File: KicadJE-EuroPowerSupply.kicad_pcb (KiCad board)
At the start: 2 copper layers, 100 x 100 mm, 115 parts, among them J101 Laptop Power, J102 +-15V thru, J103 +-12v out, J104 +5V out, J105 Laptop Power Out, P101 Doepfer_Power_10pin, P102 Doepfer_Power_16pin, P103 Doepfer_Power_10pin, P104 Doepfer_Power_16pin, P105 Doepfer_Power_10pin, P106 Doepfer_Power_16pin, P107 Doepfer_Power_10pin, P108 Doepfer_Power_16pin, Q201 TIP41, Q202 TIP41, Q203 TIP42, SW101 SW_SPDT, U201 LM7812_TO220, U202 LM7805_TO220, U203 Step Down Module +15 to 7v - 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, U204 LM7912_TO220, U205 XL6009 Module DCDC 19 to 30v, U206 TL071, U207 LM78M05_TO252, U208 LM78M12_TO252, U209 MC79M12_TO252, U210 MT3608 Module DCDC 19 to 28v

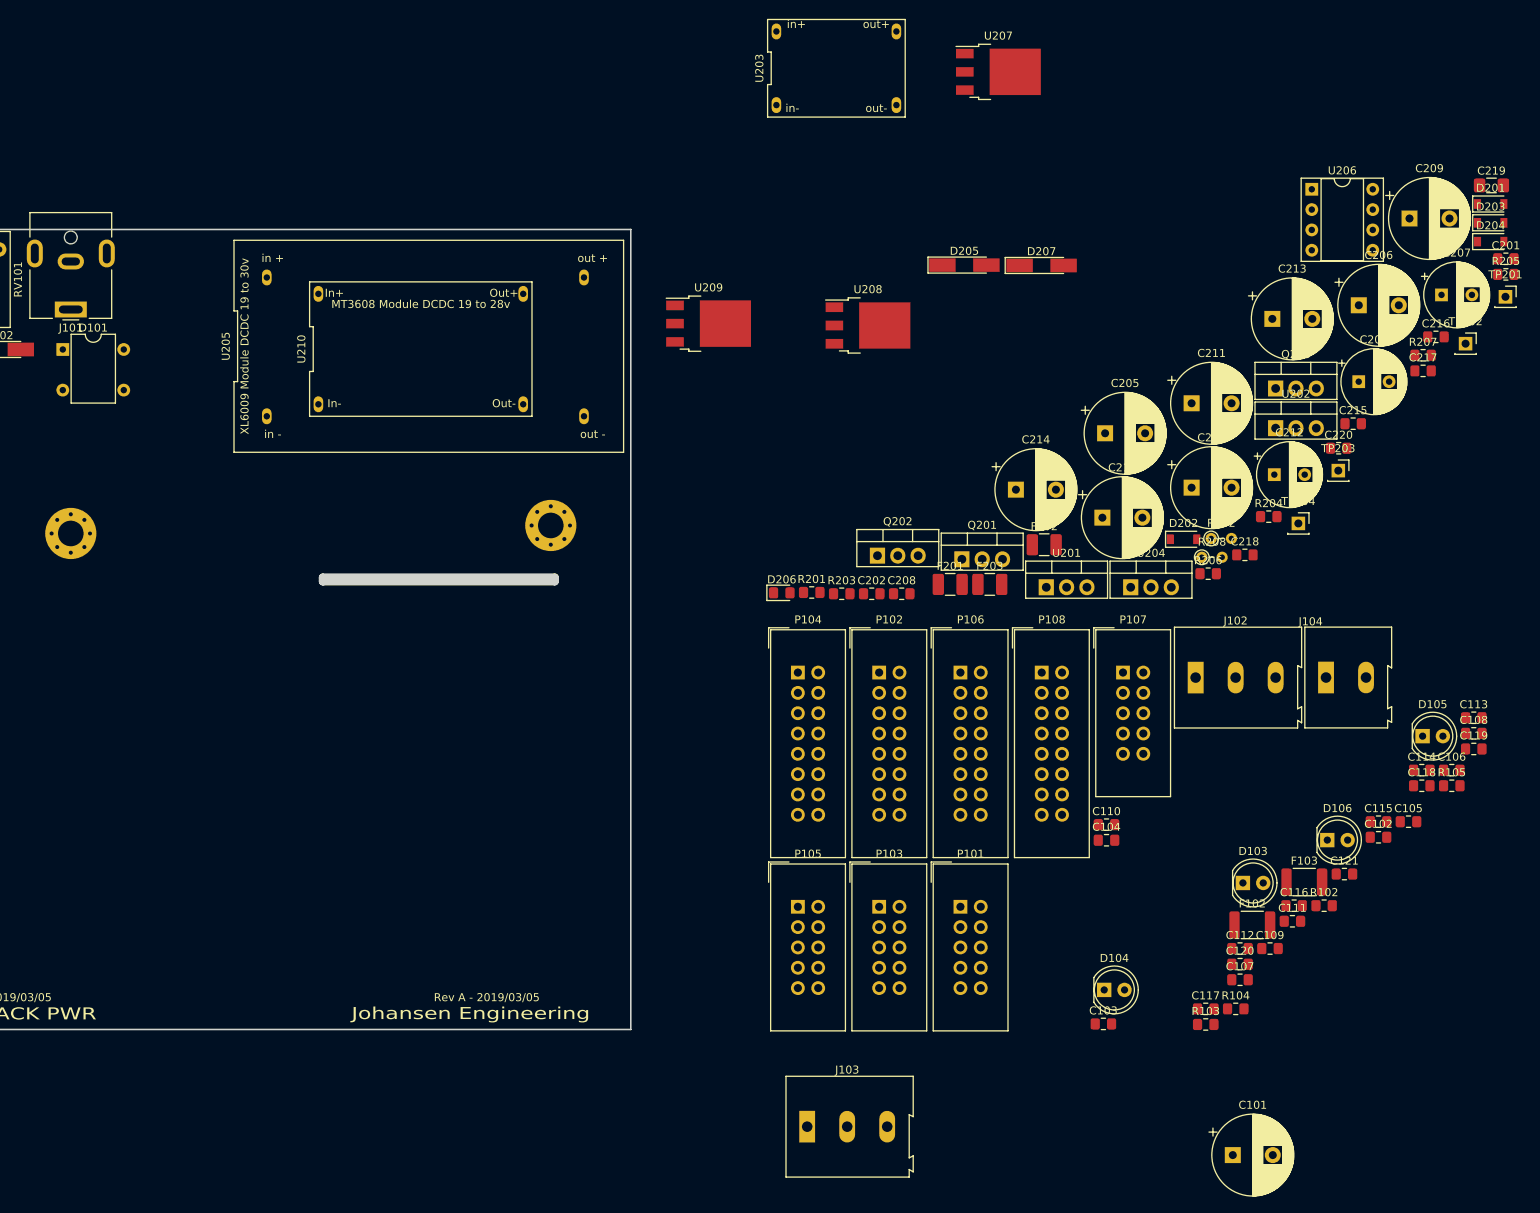
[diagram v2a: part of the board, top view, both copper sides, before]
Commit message: cut down to 2x10p and 2x16p
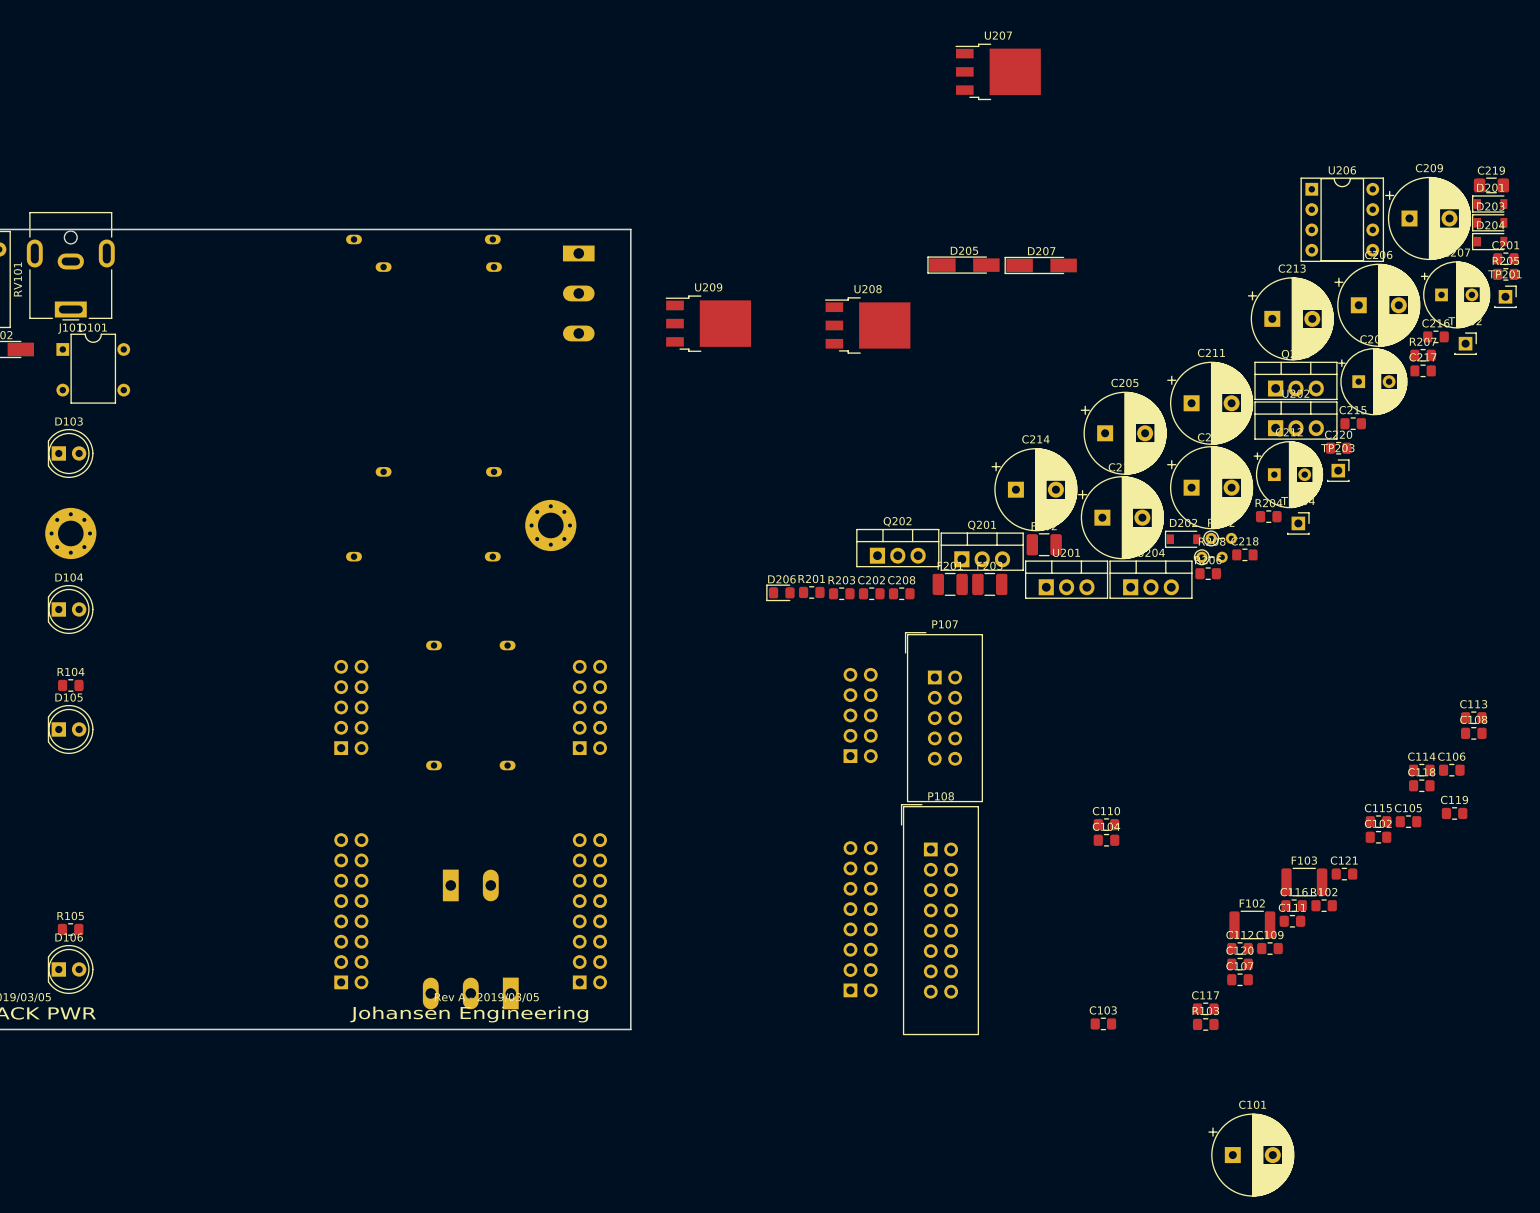
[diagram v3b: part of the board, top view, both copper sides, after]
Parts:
- J102, J103, J104, P101, P102, P103, P104, P105, P106, U203, U205, U210: moved to B.Cu
- moved R105 173.6 mm to (130.0, 137.5)
- moved D105 170.5 mm to (128.5, 112.5)
- moved D106 159.4 mm to (128.5, 142.5)
- moved D103 157.5 mm to (128.5, 78.0)
- moved R104 151.1 mm to (130.0, 107.0)
- moved D104 139.1 mm to (128.5, 97.5)
- moved J104 112.5 mm to (177.5, 132.0)
- moved J102 93.6 mm to (193.5, 53.0), turned to 270 degrees
- moved U203 91.8 mm to (180.0, 109.5), turned to 270 degrees
- moved P104 69.0 mm to (163.8, 144.1)
- moved P106 61.4 mm to (193.6, 144.1)
- moved P105 60.4 mm to (163.8, 114.8)
- moved P101 51.6 mm to (193.6, 114.8)
- moved J103 40.6 mm to (185.0, 145.5), turned to 180 degrees
- moved P102 39.9 mm to (227.5, 145.1)
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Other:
- outline, holes or cut-outs redrawn

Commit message: 3D Jigzaw started 90degr
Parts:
- removed C106, C107, C108, C109, C110, C111, C118, C119, C120, C121: 100n, Capacitor_SMD:C_0805_2012Metric_Pad1.15x1.40mm_HandSolder
- removed C211, C213: 1000uF, Capacitor_THT:CP_Radial_D10.0mm_P5.00mm
- removed P103, P107: Doepfer_Power_10pin, Connectors_IDC:IDC-Header_2x05_Pitch2.54mm_Straight
- removed P104, P108: Doepfer_Power_16pin, Connectors_IDC:IDC-Header_2x08_Pitch2.54mm_Straight
- removed REF** (x2): MountingHole_3.2mm_M3_Pad_Via, MountingHole:MountingHole_3.2mm_M3_Pad_Via
- added FL201: EMI_Filter_CommonMode, Inductor_THT:L_CommonMode_Toroid_Vertical_L19.3mm_W10.8mm_Px6.35mm_Py15.24mm_Bourns_8100, F.Cu at (99.0, -26.0)
- added FL202: EMI_Filter_CommonMode, Inductor_THT:L_CommonMode_Toroid_Vertical_L19.3mm_W10.8mm_Px6.35mm_Py15.24mm_Bourns_8100, F.Cu at (186.0, -25.5)
- added FL203: EMI_Filter_CommonMode, Inductor_THT:L_CommonMode_Toroid_Vertical_L19.3mm_W10.8mm_Px6.35mm_Py15.24mm_Bourns_8100, F.Cu at (140.7, -25.0)
- C203, C205, C210: value 1000uF -> 1u; footprint Capacitor_THT:CP_Radial_D10.0mm_P5.00mm -> Capacitor_SMD:C_1206_3216Metric_Pad1.42x1.75mm_HandSolder
- D206, R205: moved to B.Cu
- moved C201 241.3 mm to (95.0, -57.0)
- moved D201 237.2 mm to (96.0, -60.5)
- moved C204 226.9 mm to (92.0, -40.0)
- moved U201 216.5 mm to (93.4, -52.8)
- moved C206 212.0 mm to (104.0, -40.5)
- moved F201 208.7 mm to (103.5, -63.5)
- moved D203 208.6 mm to (139.5, -74.5), turned to 180 degrees
- moved F203 206.1 mm to (139.0, -82.5)
- moved U204 204.9 mm to (134.5, -65.3)
- moved C203 203.9 mm to (100.5, -31.0)
- moved TP202 196.0 mm to (112.0, 26.5)
- moved TP201 193.0 mm to (118.5, 29.5)
- moved C212 187.4 mm to (140.0, -43.5)
- moved TP203 179.6 mm to (118.5, 22.0)
- moved C215 179.5 mm to (149.0, -36.5)
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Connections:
- C205 pad 1: Net-(C205-Pad1) -> /VoltageRegulation/7V
- C205 pad 2: GND -> /VoltageRegulation/GND-7V
- C206 pad 1: Net-(C205-Pad1) -> +12V
- C208 pad 1: Net-(C208-Pad1) -> 5Vreg
- C210 pad 1: /VoltageRegulation/7V -> VinGND
- C210 pad 2: /VoltageRegulation/GND-7V -> Vin-15
- C214 pad 2: Net-(C213-Pad2) -> -12V
- D201 pad 2: Net-(C205-Pad1) -> 12Vreg
- D202 pad 2: Net-(C208-Pad1) -> 5Vreg
- D203 pad 1: Net-(C213-Pad2) -> -12Vreg
- F201 pad 1: Net-(C205-Pad1) -> 12Vreg
- F201 pad 2: Net-(C205-Pad1) -> +12V
- F202 pad 1: Net-(C208-Pad1) -> 5Vreg
- F203 pad 1: Net-(C213-Pad2) -> -12Vreg
- F203 pad 2: Net-(C213-Pad2) -> -12V
- U201 pad 3: Net-(C205-Pad1) -> 12Vreg
- U202 pad 3: Net-(C208-Pad1) -> 5Vreg
- U204 pad 3: Net-(C213-Pad2) -> -12Vreg
- U207 pad 3: +5V -> 5Vreg
- U208 pad 3: +12V -> 12Vreg
- U209 pad 3: -12V -> -12Vreg
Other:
- outline, holes or cut-outs redrawn

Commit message: Update KicadJE-EuroPowerSupply.kicad_pcb
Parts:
- added J106: FrontInterConnVin, AJ-Dropbox-Kicad:BoardConnector2x2.54x10mm2pin, F.Cu at (146.8, 85.8)
- added J107: BaseInterConnVin, AJ-Dropbox-Kicad:BoardConnector2x2.54x10mm2pin, F.Cu at (121.2, 85.6)
- added J108: FrontInterConnVout, AJ-Dropbox-Kicad:BoardConnector2x2.54x10mm4pin, F.Cu at (146.8, 129.1)
- added J109: BaseInterConnVout, AJ-Dropbox-Kicad:BoardConnector2x2.54x10mm4pin, F.Cu at (121.2, 129.1)
- moved C202 173.3 mm to (254.5, 134.3)
- moved C205 173.3 mm to (237.5, 117.3)
- moved C207 173.3 mm to (252.8, 123.5)
- moved C209 173.3 mm to (239.5, 128.8)
- moved FL202 173.3 mm to (233.0, 141.3)
- moved C216 59.2 mm to (235.5, 57.5)
- moved C217 59.2 mm to (237.5, 32.5)
- moved C220 59.2 mm to (246.0, 47.3)
- moved Q202 59.2 mm to (233.3, 40.8)
- moved Q203 59.2 mm to (254.5, 41.0)
- moved R202 59.2 mm to (246.0, 22.6)
- moved R204 59.2 mm to (253.2, 19.9)
- moved R206 59.2 mm to (245.7, 27.0)
- moved R207 59.2 mm to (237.5, 61.5)
- moved R208 59.2 mm to (244.9, 25.0)
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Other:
- board text added: "EURORACK PWR19"
- board text removed: "EURORACK PWR"

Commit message: Init wiring
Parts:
- added REF**: BoardConnector2x2.54x10mm2pin, AJ-Dropbox-Kicad:BoardConnector2x2.54x10mm2pin, F.Cu at (0.00, 0.00)
- moved FL202 22.6 mm to (224.0, 162.0), turned to 180 degrees
- moved J101 20.0 mm to (110.0, 60.4)
- moved J105 20.0 mm to (130.0, 60.4)
- moved F101 13.0 mm to (120.0, 66.0), turned to 0 degrees
- moved D102 10.8 mm to (117.0, 55.0), turned to 90 degrees
- moved D101 7.28 mm to (127.0, 72.0), turned to 90 degrees
- moved R101 4.24 mm to (117.0, 62.0), turned to 90 degrees
- moved U205 1.30 mm to (164.8, 74.5)
- moved J107 1.00 mm to (122.2, 85.6)
- moved J109 1.00 mm to (122.2, 129.1)
- moved RV101 1.00 mm to (120.0, 60.0)
- moved R102 0.71 mm to (136.0, 77.0), turned to 270 degrees
- moved J106 0.27 mm to (146.8, 85.5), turned to 270 degrees
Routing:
- net Net-(D101-Pad3): track 0.00 -> 49.4 mm
- net Net-(D103-Pad2): track 0.00 -> 4.97 mm
- net Net-(D102-Pad1): track 0.00 -> 3.23 mm

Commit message: Update KicadJE-EuroPowerSupply.kicad_pcb
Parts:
- moved C112 34.0 mm to (181.5, 119.8), turned to 90 degrees
- moved C103 30.9 mm to (190.3, 95.5)
- moved C116 29.6 mm to (190.3, 103.0), turned to 90 degrees
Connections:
- net Net-(D101-Pad3) renamed /DCSleeve
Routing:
- net +12V: track 0.00 -> 136.2 mm, vias 0 -> 2
- net +5V: track 0.00 -> 55.4 mm, vias 0 -> 2
- net -12V: track 0.00 -> 37.4 mm
- net Net-(F101-Pad1): track 0.00 -> 34.9 mm
- net Net-(D101-Pad4): track 0.00 -> 33.7 mm
- net Vin-Pos19: track 0.00 -> 27.6 mm
- net Vin-Neg19: track 0.00 -> 22.5 mm
- net Net-(J101-Pad1): track 0.00 -> 20.0 mm
- net GND: track 0.00 -> 16.8 mm, vias 0 -> 16
- net Net-(D106-Pad1): track 0.00 -> 6.04 mm
- net Net-(D105-Pad2): track 0.00 -> 5.51 mm
- net /DCSleeve: track 49.4 -> 51.8 mm
- net (no net): vias 0 -> 3
- added copper zone on B.Cu, net GND
- added copper zone on F.Cu, net GND

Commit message: Components placed on PCB - common modes removed
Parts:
- removed FL201, FL202, FL203: EMI_Filter_CommonMode, Inductor_THT:L_CommonMode_Toroid_Vertical_L19.3mm_W10.8mm_Px6.35mm_Py15.24mm_Bourns_8100
- removed REF**: BoardConnector2x2.54x10mm2pin, AJ-Dropbox-Kicad:BoardConnector2x2.54x10mm2pin
- removed TP201, TP203: VGnd, Connector_PinSocket_2.54mm:PinSocket_1x01_P2.54mm_Vertical
- removed TP202: Vin+15, Connector_PinSocket_2.54mm:PinSocket_1x01_P2.54mm_Vertical
- removed TP204: Vin-15, Connector_PinSocket_2.54mm:PinSocket_1x01_P2.54mm_Vertical
- C206, C209, C212, C214: moved to B.Cu
- D205, D207: footprint Diode_SMD:D_MiniMELF_Handsoldering -> Diode_SMD:D_MiniMELF
- moved F203 190.7 mm to (177.8, 135.5)
- moved D203 175.1 mm to (163.2, 129.8), turned to 90 degrees
- moved C214 170.5 mm to (157.2, 134.5), turned to 270 degrees
- moved F201 170.4 mm to (177.5, 123.8)
- moved U204 164.9 mm to (166.0, 127.8), turned to 270 degrees
- moved D201 160.4 mm to (163.5, 118.5), turned to 270 degrees
- moved C201 158.1 mm to (168.2, 117.2), turned to 270 degrees
- moved U209 155.9 mm to (174.5, 130.3)
- moved U208 154.1 mm to (174.4, 118.6)
- moved U201 152.8 mm to (166.0, 116.0), turned to 270 degrees
- moved C212 142.1 mm to (172.5, 126.2), turned to 270 degrees
- moved C206 141.9 mm to (157.2, 123.8), turned to 270 degrees
- moved C215 136.1 mm to (168.2, 129.0), turned to 270 degrees
- moved C204 131.5 mm to (158.2, 108.2), turned to 270 degrees
- moved C218 119.6 mm to (156.5, 99.0), turned to 270 degrees
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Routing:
- net +5V: track 55.4 -> 64.0 mm
- net +12V: track 136.2 -> 139.0 mm, vias 2 -> 3
- net GND: vias 16 -> 18
- net -12V: vias 0 -> 2
- net (no net): vias 3 -> 0
